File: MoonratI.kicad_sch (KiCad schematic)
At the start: 13 parts

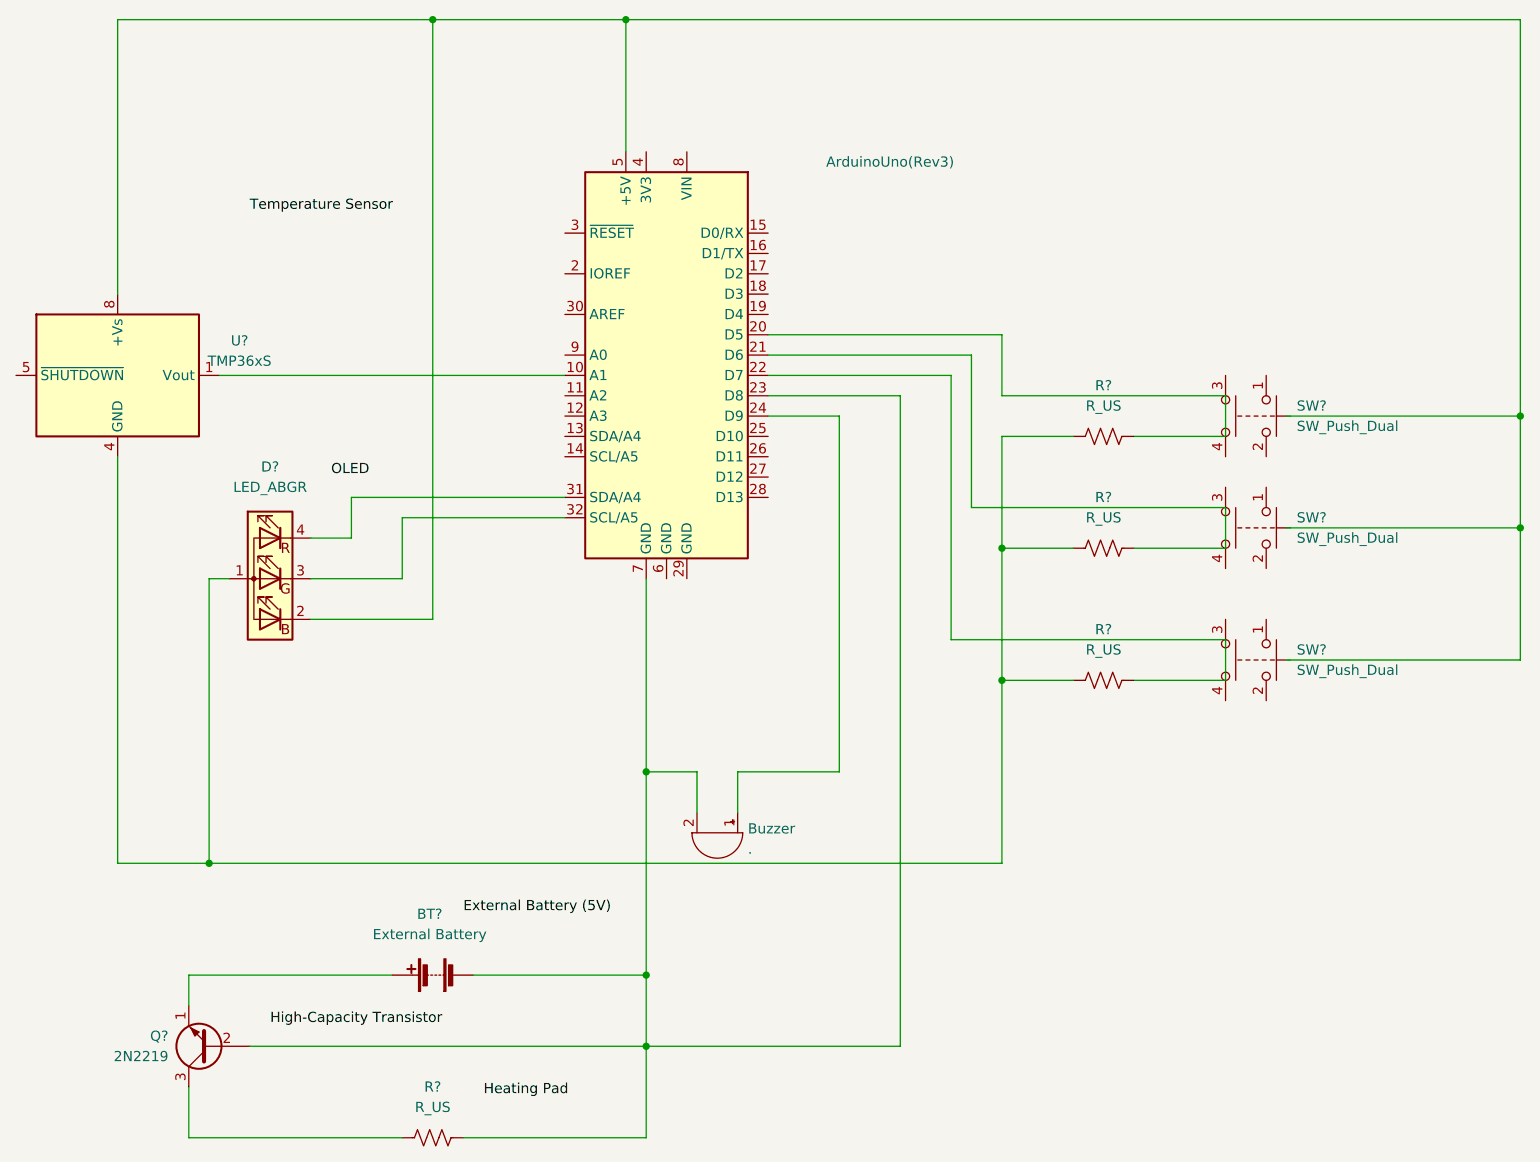
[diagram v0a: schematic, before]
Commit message: annotated schematic with reset.
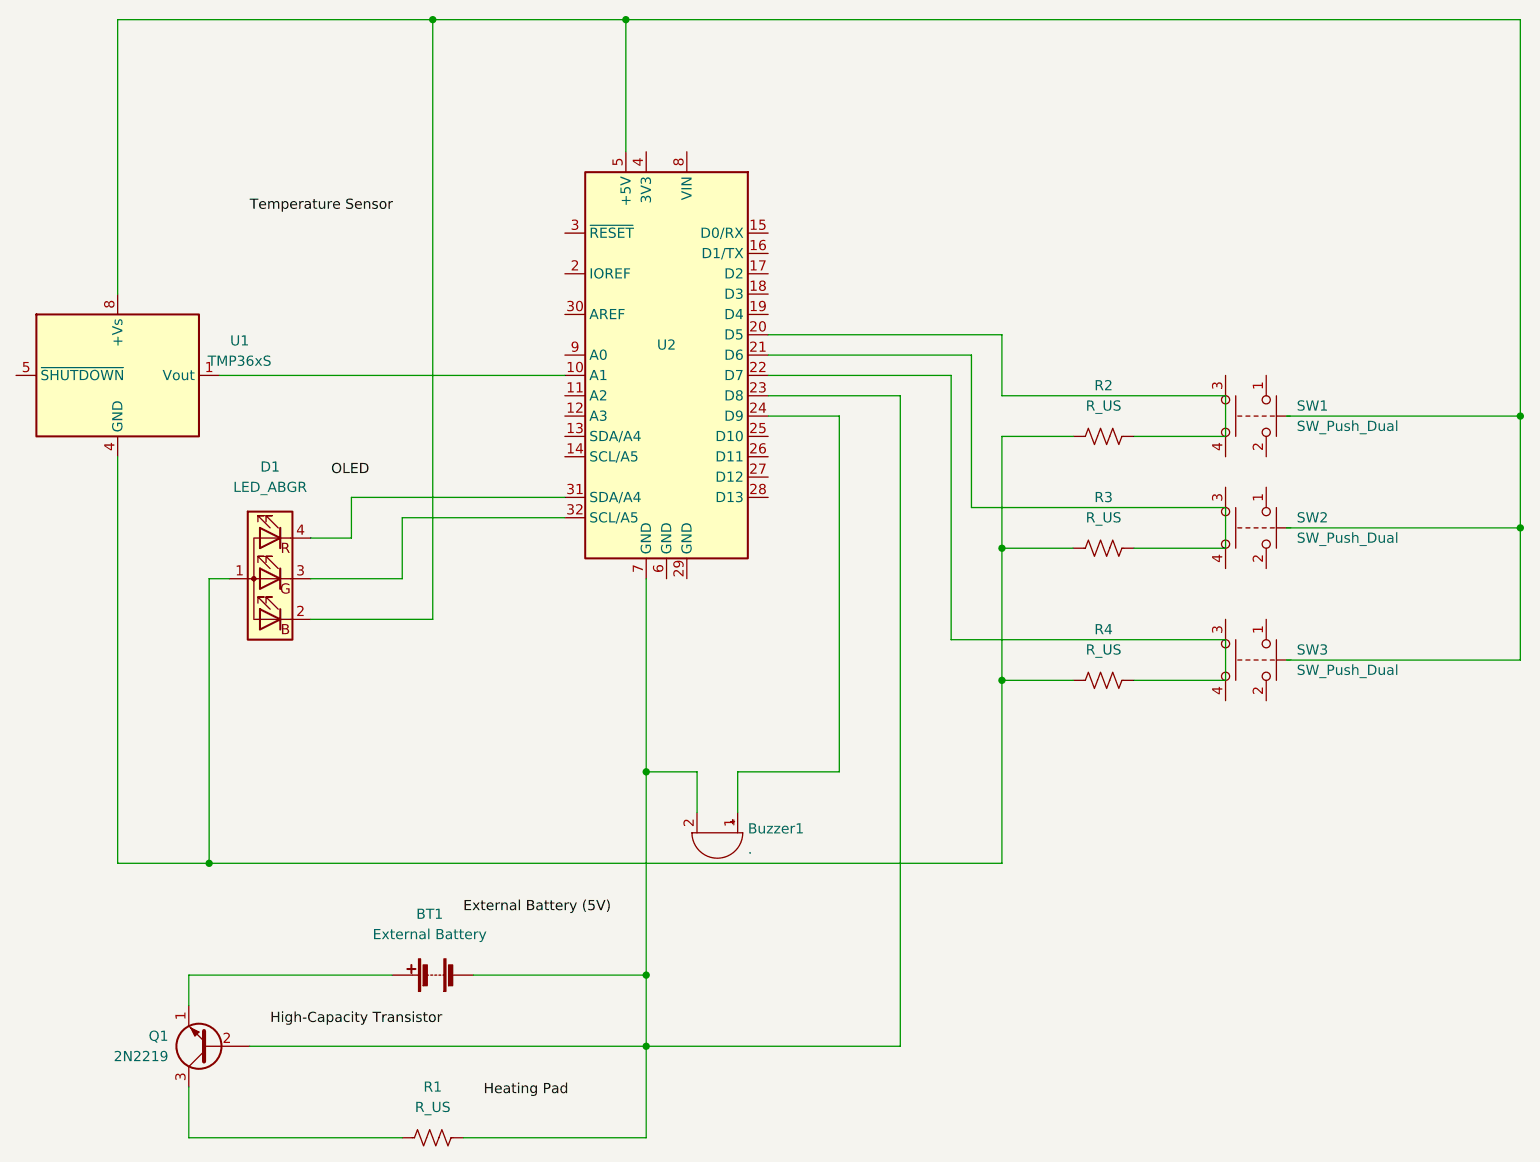
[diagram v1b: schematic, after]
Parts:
- gave numbers to parts that had none: 11
- renumbered Buzzer to Buzzer1, ArduinoUno(Rev3) to U2
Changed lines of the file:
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@@
   (symbol (lib_id "Sensor_Temperature:TMP36xS") (at 59.69 83.82 0) (unit 1)
     (in_bom yes) (on_board yes) (fields_autoplaced)
-    (property "Reference" "U?" (id 0) (at 74.93 79.4893 0))
+    (property "Reference" "U1" (id 0) (at 74.93 79.4893 0))
     (property "Value" "TMP36xS" (id 1) (at 74.93 82.0293 0))
     (property "Footprint" "Package_SO:SOIC-8_3.9x4.9mm_P1.27mm" (id 2) (at 59.69 95.25 0)
@@
   (symbol (lib_id "Device:R_US") (at 182.88 105.41 270) (unit 1)
     (in_bom yes) (on_board yes) (fields_autoplaced)
-    (property "Reference" "R?" (id 0) (at 182.88 99.06 90))
+    (property "Reference" "R3" (id 0) (at 182.88 99.06 90))
     (property "Value" "R_US" (id 1) (at 182.88 101.6 90))
     (property "Footprint" "" (id 2) (at 182.626 106.426 90)
@@
   (symbol (lib_id "Switch:SW_Push_Dual") (at 203.2 102.87 270) (unit 1)
     (in_bom yes) (on_board yes) (fields_autoplaced)
-    (property "Reference" "SW?" (id 0) (at 207.01 101.5999 90)
+    (property "Reference" "SW2" (id 0) (at 207.01 101.5999 90)
       (effects (font (size 1.27 1.27)) (justify left))
     )
@@
   (symbol (lib_id "Switch:SW_Push_Dual") (at 203.2 119.38 270) (unit 1)
     (in_bom yes) (on_board yes) (fields_autoplaced)
-    (property "Reference" "SW?" (id 0) (at 207.01 118.1099 90)
+    (property "Reference" "SW3" (id 0) (at 207.01 118.1099 90)
       (effects (font (size 1.27 1.27)) (justify left))
     )
@@
   (symbol (lib_id "Switch:SW_Push_Dual") (at 203.2 88.9 270) (unit 1)
     (in_bom yes) (on_board yes) (fields_autoplaced)
-    (property "Reference" "SW?" (id 0) (at 207.01 87.6299 90)
+    (property "Reference" "SW1" (id 0) (at 207.01 87.6299 90)
       (effects (font (size 1.27 1.27)) (justify left))
     )
@@
   (symbol (lib_id "Device:LED_ABGR") (at 78.74 109.22 0) (mirror y) (unit 1)
     (in_bom yes) (on_board yes) (fields_autoplaced)
-    (property "Reference" "D?" (id 0) (at 78.74 95.25 0))
+    (property "Reference" "D1" (id 0) (at 78.74 95.25 0))
     (property "Value" "LED_ABGR" (id 1) (at 78.74 97.79 0))
     (property "Footprint" "" (id 2) (at 78.74 110.49 0)
@@
   (symbol (lib_id "Device:R_US") (at 182.88 91.44 270) (unit 1)
     (in_bom yes) (on_board yes) (fields_autoplaced)
-    (property "Reference" "R?" (id 0) (at 182.88 85.09 90))
+    (property "Reference" "R2" (id 0) (at 182.88 85.09 90))
     (property "Value" "R_US" (id 1) (at 182.88 87.63 90))
     (property "Footprint" "" (id 2) (at 182.626 92.456 90)
@@
   (symbol (lib_id "Device:Battery") (at 99.06 158.75 90) (unit 1)
     (in_bom yes) (on_board yes) (fields_autoplaced)
-    (property "Reference" "BT?" (id 0) (at 98.679 151.13 90))
+    (property "Reference" "BT1" (id 0) (at 98.679 151.13 90))
     (property "Value" "External Battery" (id 1) (at 98.679 153.67 90))
     (property "Footprint" "" (id 2) (at 97.536 158.75 90)
@@
   (symbol (lib_id "Device:Buzzer") (at 134.62 140.97 270) (unit 1)
     (in_bom yes) (on_board yes) (fields_autoplaced)
-    (property "Reference" "Buzzer" (id 0) (at 138.43 140.4619 90)
+    (property "Reference" "Buzzer1" (id 0) (at 138.43 140.4619 90)
       (effects (font (size 1.27 1.27)) (justify left))
     )
@@
   (symbol (lib_id "Device:R_US") (at 99.06 179.07 270) (unit 1)
     (in_bom yes) (on_board yes) (fields_autoplaced)
-    (property "Reference" "R?" (id 0) (at 99.06 172.72 90))
+    (property "Reference" "R1" (id 0) (at 99.06 172.72 90))
     (property "Value" "R_US" (id 1) (at 99.06 175.26 90))
     (property "Footprint" "" (id 2) (at 98.806 180.086 90)
@@
   (symbol (lib_id "Transistor_BJT:2N2219") (at 71.12 167.64 180) (unit 1)
     (in_bom yes) (on_board yes) (fields_autoplaced)
-    (property "Reference" "Q?" (id 0) (at 66.04 166.3699 0)
+    (property "Reference" "Q1" (id 0) (at 66.04 166.3699 0)
       (effects (font (size 1.27 1.27)) (justify left))
     )
@@
   (symbol (lib_id "Device:R_US") (at 182.88 121.92 270) (unit 1)
     (in_bom yes) (on_board yes) (fields_autoplaced)
-    (property "Reference" "R?" (id 0) (at 182.88 115.57 90))
+    (property "Reference" "R4" (id 0) (at 182.88 115.57 90))
     (property "Value" "R_US" (id 1) (at 182.88 118.11 90))
     (property "Footprint" "" (id 2) (at 182.626 122.936 90)
@@
   (symbol (lib_id "MCU_Module:Arduino_UNO_R3") (at 128.27 81.28 0) (mirror y) (unit 1)
     (in_bom yes) (on_board yes)
-    (property "Reference" "ArduinoUno(Rev3)" (id 0) (at 156.21 57.15 0))
+    (property "Reference" "U2" (id 0) (at 128.27 80.01 0))
     (property "Value" "Arduino_UNO_R3" (id 1) (at 121.1706 55.88 0)
       (effects (font (size 1.27 1.27)) hide)
@@
   )
   (symbol_instances
+    (path "/8b011396-441b-44c2-b1ef-7003afad6f4f"
+      (reference "BT1") (unit 1) (value "External Battery") (footprint "")
+    )
+    (path "/9cc8e80e-8f0e-4192-ad35-fc9ad8f898fb"
+      (reference "Buzzer1") (unit 1) (value ".") (footprint "")
+    )
+    (path "/41eec197-6044-43f0-ad61-ea40fba67838"
+      (reference "D1") (unit 1) (value "LED_ABGR") (footprint "")
+    )
+    (path "/a920a4c2-8a4b-4324-bfef-128c0184ef5a"
+      (reference "Q1") (unit 1) (value "2N2219") (footprint "Package_TO_SOT_THT:TO-39-3")
+    )
+    (path "/a2f32991-c2be-48a5-a3d7-5db6d3cf0e56"
+      (reference "R1") (unit 1) (value "R_US") (footprint "")
+    )
+    (path "/4791376b-b2e1-4d69-a8e0-b9ac9fd714e9"
+      (reference "R2") (unit 1) (value "R_US") (footprint "")
+    )
+    (path "/09fc1d9d-738a-46e5-8aa8-9900384dae68"
+      (reference "R3") (unit 1) (value "R_US") (footprint "")
+    )
+    (path "/b3ebea10-0068-4fb3-84ee-e9bf4f4344ac"
+      (reference "R4") (unit 1) (value "R_US") (footprint "")
+    )
+    (path "/3f335709-bc57-4daa-b314-c9210f1957ec"
+      (reference "SW1") (unit 1) (value "SW_Push_Dual") (footprint "")
+    )
+    (path "/296fb7aa-4066-4ca7-a4d9-928b3214edb3"
+      (reference "SW2") (unit 1) (value "SW_Push_Dual") (footprint "")
+    )
+    (path "/3058c7a8-5d7f-4a0c-998e-562eb23cdaa7"
+      (reference "SW3") (unit 1) (value "SW_Push_Dual") (footprint "")
+    )
+    (path "/091ccf89-1082-40c2-812c-090b6fd0c1d8"
+      (reference "U1") (unit 1) (value "TMP36xS") (footprint "Package_SO:SOIC-8_3.9x4.9mm_P1.27mm")
+    )
     (path "/da00102b-a23b-40d9-90f7-698e51724f30"
-      (reference "ArduinoUno(Rev3)") (unit 1) (value "Arduino_UNO_R3") (footprint "Module:Arduino_UNO_R3")
-    )
-    (path "/8b011396-441b-44c2-b1ef-7003afad6f4f"
-      (reference "BT?") (unit 1) (value "External Battery") (footprint "")
-    )
-    (path "/9cc8e80e-8f0e-4192-ad35-fc9ad8f898fb"
-      (reference "Buzzer") (unit 1) (value ".") (footprint "")
-    )
-    (path "/41eec197-6044-43f0-ad61-ea40fba67838"
-      (reference "D?") (unit 1) (value "LED_ABGR") (footprint "")
-    )
-    (path "/a920a4c2-8a4b-4324-bfef-128c0184ef5a"
-      (reference "Q?") (unit 1) (value "2N2219") (footprint "Package_TO_SOT_THT:TO-39-3")
-    )
-    (path "/09fc1d9d-738a-46e5-8aa8-9900384dae68"
-      (reference "R?") (unit 1) (value "R_US") (footprint "")
-    )
-    (path "/4791376b-b2e1-4d69-a8e0-b9ac9fd714e9"
-      (reference "R?") (unit 1) (value "R_US") (footprint "")
-    )
-    (path "/a2f32991-c2be-48a5-a3d7-5db6d3cf0e56"
-      (reference "R?") (unit 1) (value "R_US") (footprint "")
-    )
-    (path "/b3ebea10-0068-4fb3-84ee-e9bf4f4344ac"
-      (reference "R?") (unit 1) (value "R_US") (footprint "")
-    )
-    (path "/296fb7aa-4066-4ca7-a4d9-928b3214edb3"
-      (reference "SW?") (unit 1) (value "SW_Push_Dual") (footprint "")
-    )
-    (path "/3058c7a8-5d7f-4a0c-998e-562eb23cdaa7"
-      (reference "SW?") (unit 1) (value "SW_Push_Dual") (footprint "")
-    )
-    (path "/3f335709-bc57-4daa-b314-c9210f1957ec"
-      (reference "SW?") (unit 1) (value "SW_Push_Dual") (footprint "")
-    )
-    (path "/091ccf89-1082-40c2-812c-090b6fd0c1d8"
-      (reference "U?") (unit 1) (value "TMP36xS") (footprint "Package_SO:SOIC-8_3.9x4.9mm_P1.27mm")
-    )
-  )
+      (reference "U2") (unit 1) (value "Arduino_UNO_R3") (footprint "Module:Arduino_UNO_R3")
+    )
+  )
